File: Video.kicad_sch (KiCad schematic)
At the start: 53 parts, among them Q10 2N3904, Q6 2N3904, Q7 2N3904, Q8 2N3904, Q9 2N3904, U13 74HCT14D, U15 74HC86, U40 GST_SHIFTER, U41 74LS257, U42 GST_MCU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

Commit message: motherboard: Added more footprints for parts and refined the serial comms section further
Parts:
- U41: footprint (none) -> Package_SO:TSSOP-16_4.4x5mm_P0.65mm; MFR (none) -> Nexperia; MPN (none) -> 74HC257PW,118; OC_FARNELL (none) -> 2445284
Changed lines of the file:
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@@
 			)
 		)
-		(property "Footprint" ""
+		(property "Footprint" "Package_SO:TSSOP-16_4.4x5mm_P0.65mm"
 			(at 355.6 76.2 0)
 			(effects
@@
 			(at 355.6 76.2 0)
 			(effects
+				(font
+					(size 1.27 1.27)
+				)
+				(hide yes)
+			)
+		)
+		(property "MFR" "Nexperia"
+			(at 355.6 76.2 0)
+			(effects
+				(font
+					(size 1.27 1.27)
+				)
+				(hide yes)
+			)
+		)
+		(property "MPN" "74HC257PW,118"
+			(at 355.6 76.2 0)
+			(effects
+				(font
+					(size 1.27 1.27)
+				)
+				(hide yes)
+			)
+		)
+		(property "OC_FARNELL" "2445284"
+			(at 355.6 76.2 0)
+			(effects

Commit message: motherboard: Sorted out all the 1N914's having found a suitable part
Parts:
- D8, D9: footprint (none) -> Diode_SMD:D_SOD-323F; MFR (none) -> Onsemi; MPN (none) -> 1N914BWS; OC_FARNELL (none) -> 2453274
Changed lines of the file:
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@@
 			)
 		)
-		(property "Footprint" ""
+		(property "Footprint" "Diode_SMD:D_SOD-323F"
 			(at 238.76 227.33 90)
 			(effects
@@
 			)
 		)
-		(property "Datasheet" "~"
+		(property "Datasheet" "https://www.onsemi.com/download/data-sheet/pdf/1n4148ws-d.pdf"
 			(at 238.76 227.33 90)
 			(effects
@@
 			)
 		)
-		(property "MFR" ""
+		(property "MFR" "Onsemi"
 			(at 238.76 227.33 0)
 			(effects
@@
 			)
 		)
-		(property "MPN" ""
+		(property "MPN" "1N914BWS"
 			(at 238.76 227.33 0)
 			(effects
@@
 			)
 		)
-		(property "OC_FARNELL" ""
+		(property "OC_FARNELL" "2453274"
 			(at 238.76 227.33 0)
 			(effects
@@
 			)
 		)
-		(property "Footprint" ""
+		(property "Footprint" "Diode_SMD:D_SOD-323F"
 			(at 238.76 220.98 90)
 			(effects
@@
 			)
 		)
-		(property "Datasheet" "~"
+		(property "Datasheet" "https://www.onsemi.com/download/data-sheet/pdf/1n4148ws-d.pdf"
 			(at 238.76 220.98 90)
 			(effects
@@
 			)
 		)
-		(property "MFR" ""
+		(property "MFR" "Onsemi"
 			(at 238.76 220.98 0)
 			(effects
@@
 			)
 		)
-		(property "MPN" ""
+		(property "MPN" "1N914BWS"
 			(at 238.76 220.98 0)
 			(effects
@@
 			)
 		)
-		(property "OC_FARNELL" ""
+		(property "OC_FARNELL" "2453274"
 			(at 238.76 220.98 0)
 			(effects

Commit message: motherboard: Sorted out the connectors for the joystick ports and video port
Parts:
- added C126, C127, C128, C129, C130: 100n, rhais_rcl:C0603, symbol Device:C_Small
- added J14: Video, Connector_Dsub:DSUB-15-HD_Socket_Horizontal_P2.29x2.54mm_EdgePinOffset8.35mm_Housed_MountingHolesOffset10.89mm, symbol Connector:DE15_Socket_HighDensity
- added R126, R127: 33R, rhais_rcl:R0603, symbol Device:R_Small
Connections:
- net +5V: now also C126.1, C127.1, C128.1, C129.1, C130.1
- net GND: now also C126.2, C127.2, C128.2, C129.2, C130.2, J14.10, J14.5, J14.6, J14.7, J14.8
- net HSYNC: now also R126.2
- net ~{VSYNC}: now also R127.2
- net R: now reaches R121.2
- net R: now also J14.1
- net B: now reaches R123.2
- net B: now also J14.3
- net G: now reaches R122.2
- net G: now also J14.2
- new net: J14.13, R126.1
- new net: J14.14, R127.1
- no-connect marks 21 -> 27

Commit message: motherboard: Routed in the sound DMA output and microwire control from SHIFTER
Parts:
- removed unit 2 of U13
- added unit 1 of U13
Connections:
- net Sound.D7: now also U13.2
- net at U40.21 (SD7): now also U13.1
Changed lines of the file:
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@@
-	)
-	(symbol
-		(lib_id "74xx:74LS04")
-		(at 243.84 198.12 0)
-		(unit 2)
-		(exclude_from_sim no)
-		(in_bom yes)
-		(on_board yes)
-		(dnp no)
-		(property "Reference" "U13"
-			(at 242.824 198.12 0)
-			(effects
-				(font
-					(size 1.27 1.27)
-				)
-			)
-		)
-		(property "Value" "74HCT14D"
-			(at 246.38 201.93 0)
-			(effects
-				(font
-					(size 1.27 1.27)
-				)
-			)
-		)
-		(property "Footprint" "rhais_package-smd:SO-14_3.9x8.65mm_P1.27mm"
-			(at 243.84 198.12 0)
-			(effects
-				(font
-					(size 1.27 1.27)
-				)
-				(hide yes)
-			)
-		)
-		(property "Datasheet" "https://assets.nexperia.com/documents/data-sheet/74HC_HCT14.pdf"
-			(at 243.84 198.12 0)
-			(effects
-				(font
-					(size 1.27 1.27)
-				)
-				(hide yes)
-			)
-		)
-		(property "Description" "Hex Inverter"
-			(at 243.84 198.12 0)
-			(effects
-				(font
-					(size 1.27 1.27)
-				)
-				(hide yes)
-			)
-		)
-		(property "MFR" "Nexperia"
-			(at 243.84 198.12 0)
-			(effects
-				(font
-					(size 1.27 1.27)
-				)
-				(hide yes)
-			)
-		)
-		(property "MPN" "74HCT14D,653"
-			(at 243.84 198.12 0)
-			(effects
-				(font
-					(size 1.27 1.27)
-				)
-				(hide yes)
-			)
-		)
-		(property "OC_FARNELL" "1201304"
-			(at 243.84 198.12 0)
-			(effects
-				(font
-					(size 1.27 1.27)
-				)
-				(hide yes)
-			)
-		)
-		(pin "12"
-		)
-		(pin "10"
-		)
-		(pin "11"
-		)
-		(pin "8"
-		)
-		(pin "7"
-		)
-		(pin "13"
-		)
-		(pin "14"
-		)
-		(pin "4"
-		)
-		(pin "9"
-		)
-		(pin "2"
-		)
-		(pin "6"
-		)
-		(pin "3"
-		)
-		(pin "5"
-		)
-		(pin "1"
-		)
-		(instances
-			(project "dragonSTe"
-				(path "/6cc81c6b-09a2-4492-8ca2-d80a5c796e77/c7206c05-6723-45c2-9080-55867b906515"
-					(reference "U13")
-					(unit 2)
-				)
-			)
-		)
 	)
 	(symbol
@@
 					(unit 1)
 				)
+			)
+		)
+	)
+	(symbol
+		(lib_id "74xx:74LS04")
+		(at 243.84 198.12 0)
+		(unit 1)
+		(exclude_from_sim no)
+		(in_bom yes)
+		(on_board yes)
+		(dnp no)
+		(property "Reference" "U13"
+			(at 242.824 198.12 0)
+			(effects
+				(font
+					(size 1.27 1.27)
+				)
+			)
+		)
+		(property "Value" "74HCT14D"
+			(at 247.65 201.93 0)
+			(effects
+				(font
+					(size 1.27 1.27)
+				)
+			)
+		)
+		(property "Footprint" "rhais_package-smd:SO-14_3.9x8.65mm_P1.27mm"
+			(at 243.84 198.12 0)
+			(effects
+				(font
+					(size 1.27 1.27)
+				)
+				(hide yes)
+			)
+		)
+		(property "Datasheet" "https://assets.nexperia.com/documents/data-sheet/74HC_HCT14.pdf"
+			(at 243.84 198.12 0)
+			(effects
+				(font
+					(size 1.27 1.27)
+				)
+				(hide yes)
+			)
+		)
+		(property "Description" "Hex Inverter"
+			(at 243.84 198.12 0)
+			(effects
+				(font
+					(size 1.27 1.27)
+				)
+				(hide yes)
+			)
+		)
+		(property "MFR" "Nexperia"
+			(at 243.84 198.12 0)
+			(effects
+				(font
+					(size 1.27 1.27)
+				)
+				(hide yes)
+			)
+		)
+		(property "MPN" "74HCT14D,653"
+			(at 243.84 198.12 0)
+			(effects
+				(font
+					(size 1.27 1.27)
+				)
+				(hide yes)
+			)
+		)
+		(property "OC_FARNELL" "1201304"
+			(at 243.84 198.12 0)
+			(effects
+				(font
+					(size 1.27 1.27)
+				)
+				(hide yes)
+			)
+		)
+		(pin "12"
+		)
+		(pin "10"
+		)
+		(pin "11"
+		)
+		(pin "8"
+		)
+		(pin "7"
+		)
+		(pin "13"
+		)
+		(pin "14"
+		)
+		(pin "4"
+		)
+		(pin "9"
+		)
+		(pin "2"
+		)
+		(pin "6"
+		)
+		(pin "3"
+		)
+		(pin "5"
+		)
+		(pin "1"
+		)
+		(instances
+			(project "dragonSTe"
+				(path "/6cc81c6b-09a2-4492-8ca2-d80a5c796e77/c7206c05-6723-45c2-9080-55867b906515"
+					(reference "U13")
+					(unit 1)
+				)

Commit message: motherboard: Cleaned up the clock tree implementation, specifying and fixing down how to do the 32MHz clock source
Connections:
- net MC renamed MCLK
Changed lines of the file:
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@@
 		)
 	)
-	(label "MC"
+	(label "MCLK"
 		(at 195.58 58.42 0)
 		(effects
@@
 		)
 	)
-	(label "MC"
+	(label "MCLK"
 		(at 373.38 60.96 180)
 		(effects

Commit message: motherboard: Plumbed in MCLK to the mux and SHIFTER
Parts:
- added C132: 100n, rhais_rcl:C0603, symbol Device:C_Small
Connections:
- net +5V: now also C132.1
- net GND: now also C132.2
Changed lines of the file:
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@@
 	(wire
 		(pts
+			(xy 393.7 78.74) (xy 393.7 81.28)
+		)
+		(stroke
+			(width 0)
+			(type default)
+		)
+	)
+	(wire
+		(pts
 			(xy 104.14 177.8) (xy 109.22 177.8)
 		)
@@
 	(wire
 		(pts
+			(xy 393.7 71.12) (xy 393.7 73.66)
+		)
+		(stroke
+			(width 0)
+			(type default)
+		)
+	)
+	(wire
+		(pts
 			(xy 363.22 170.18) (xy 365.76 170.18)
 		)
@@
 	)
 	(symbol
+		(lib_id "power:+5V")
+		(at 393.7 71.12 0)
+		(unit 1)
+		(exclude_from_sim no)
+		(in_bom yes)
+		(on_board yes)
+		(dnp no)
+		(property "Reference" "#PWR0312"
+			(at 393.7 74.93 0)
+			(effects
+				(font
+					(size 1.27 1.27)
+				)
+				(hide yes)
+			)
+		)
+		(property "Value" "+5V"
+			(at 393.7 67.564 0)
+			(effects
+				(font
+					(size 1.27 1.27)
+				)
+			)
+		)
+		(property "Footprint" ""
+			(at 393.7 71.12 0)
+			(effects
+				(font
+					(size 1.27 1.27)
+				)
+				(hide yes)
+			)
+		)
+		(property "Datasheet" ""
+			(at 393.7 71.12 0)
+			(effects
+				(font
+					(size 1.27 1.27)
+				)
+				(hide yes)
+			)
+		)
+		(property "Description" "Power symbol creates a global label with name \"+5V\""
+			(at 393.7 71.12 0)
+			(effects
+				(font
+					(size 1.27 1.27)
+				)
+				(hide yes)
+			)
+		)
+		(pin "1"
+		)
+		(instances
+			(project "dragonSTe"
+				(path "/6cc81c6b-09a2-4492-8ca2-d80a5c796e77/c7206c05-6723-45c2-9080-55867b906515"
+					(reference "#PWR0312")
+					(unit 1)
+				)
+			)
+		)
+	)
+	(symbol
 		(lib_id "Device:C_Small")
 		(at 121.92 50.8 0)
@@
 	)
 	(symbol
+		(lib_id "power:GND")
+		(at 393.7 81.28 0)
+		(unit 1)
+		(exclude_from_sim no)
+		(in_bom yes)
+		(on_board yes)
+		(dnp no)
+		(property "Reference" "#PWR0313"
+			(at 393.7 87.63 0)
+			(effects
+				(font
+					(size 1.27 1.27)
+				)
+				(hide yes)
+			)
+		)
+		(property "Value" "GND"
+			(at 393.7 85.09 0)
+			(effects
+				(font
+					(size 1.27 1.27)
+				)
+			)
+		)
+		(property "Footprint" ""
+			(at 393.7 81.28 0)
+			(effects
+				(font
+					(size 1.27 1.27)
+				)
+				(hide yes)
+			)
+		)
+		(property "Datasheet" ""
+			(at 393.7 81.28 0)
+			(effects
+				(font
+					(size 1.27 1.27)
+				)
+				(hide yes)
+			)
+		)
+		(property "Description" "Power symbol creates a global label with name \"GND\" , ground"
+			(at 393.7 81.28 0)
+			(effects
+				(font
+					(size 1.27 1.27)
+				)
+				(hide yes)
+			)
+		)
+		(pin "1"
+		)
+		(instances
+			(project "dragonSTe"
+				(path "/6cc81c6b-09a2-4492-8ca2-d80a5c796e77/c7206c05-6723-45c2-9080-55867b906515"
+					(reference "#PWR0313")
+					(unit 1)
+				)
+			)
+		)
+	)
+	(symbol
 		(lib_id "Device:R_Small")
 		(at 236.22 63.5 270)
@@
 					(unit 1)
 				)
+			)
+		)
+	)
+	(symbol
+		(lib_id "Device:C_Small")
+		(at 393.7 76.2 0)
+		(unit 1)
+		(exclude_from_sim no)
+		(in_bom yes)
+		(on_board yes)
+		(dnp no)
+		(property "Reference" "C132"
+			(at 393.446 75.438 90)
+			(effects
+				(font
+					(size 1.27 1.27)
+				)
+				(justify left bottom)
+			)
+		)
+		(property "Value" "100n"
+			(at 393.446 76.708 90)
+			(effects
+				(font
+					(size 1.27 1.27)
+				)
+				(justify right bottom)
+			)
+		)
+		(property "Footprint" "rhais_rcl:C0603"
+			(at 393.7 76.2 0)
+			(effects
+				(font
+					(size 1.27 1.27)
+				)
+				(hide yes)
+			)
+		)
+		(property "Datasheet" "~"
+			(at 393.7 76.2 0)
+			(effects
+				(font
+					(size 1.27 1.27)
+				)
+				(hide yes)
+			)
+		)
+		(property "Description" "Unpolarized capacitor, small symbol"
+			(at 393.7 76.2 0)
+			(effects
+				(font
+					(size 1.27 1.27)
+				)
+				(hide yes)
+			)
+		)
+		(property "MFR" ""
+			(at 393.7 76.2 0)
+			(effects
+				(font
+					(size 1.27 1.27)
+				)
+				(hide yes)
+			)
+		)
+		(property "MPN" ""
+			(at 393.7 76.2 0)
+			(effects
+				(font
+					(size 1.27 1.27)
+				)
+				(hide yes)
+			)
+		)
+		(property "OC_FARNELL" ""
+			(at 393.7 76.2 0)
+			(effects
+				(font
+					(size 1.27 1.27)
+				)
+				(hide yes)
+			)
+		)
+		(pin "1"
+		)
+		(pin "2"
+		)
+		(instances
+			(project "dragonSTe"
+				(path "/6cc81c6b-09a2-4492-8ca2-d80a5c796e77/c7206c05-6723-45c2-9080-55867b906515"
+					(reference "C132")
+					(unit 1)
+				)

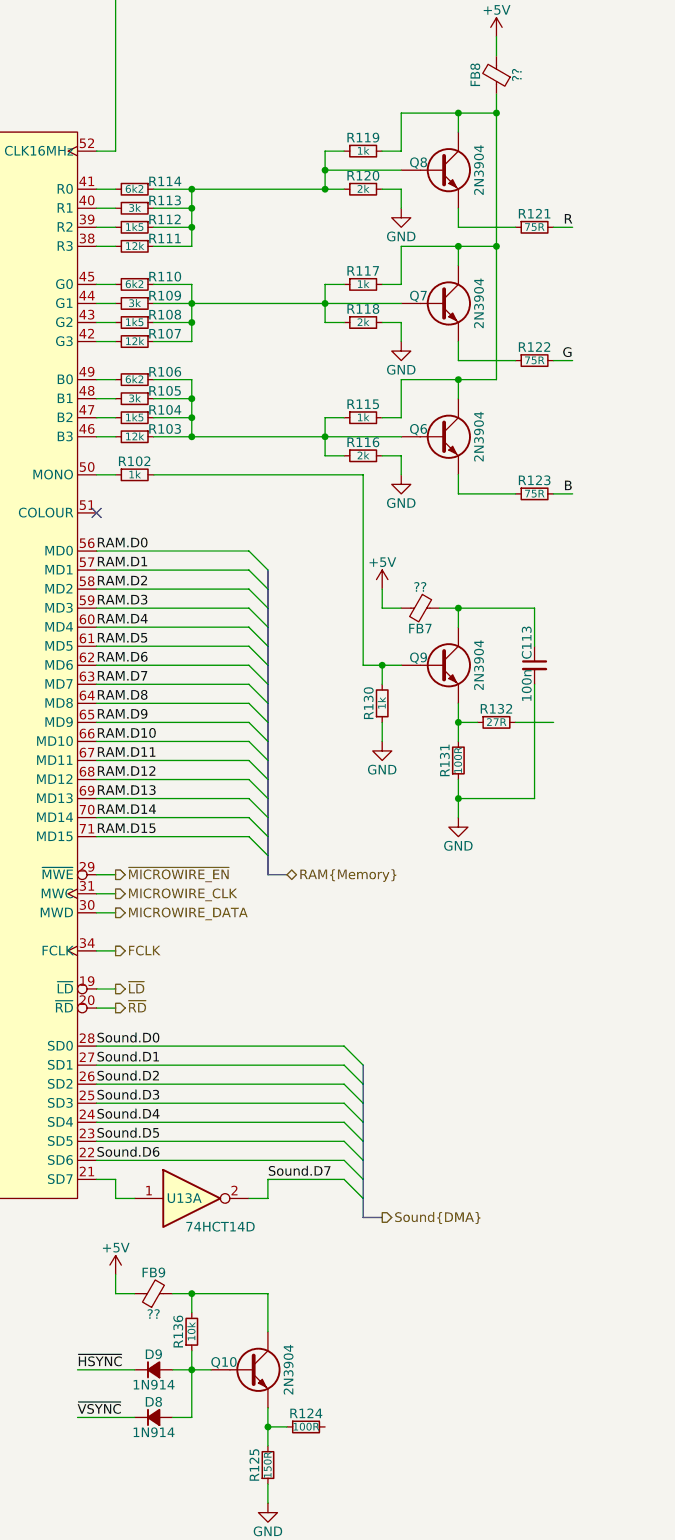
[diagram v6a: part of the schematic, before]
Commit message: motherboard: Routed the video output from SHIFTER
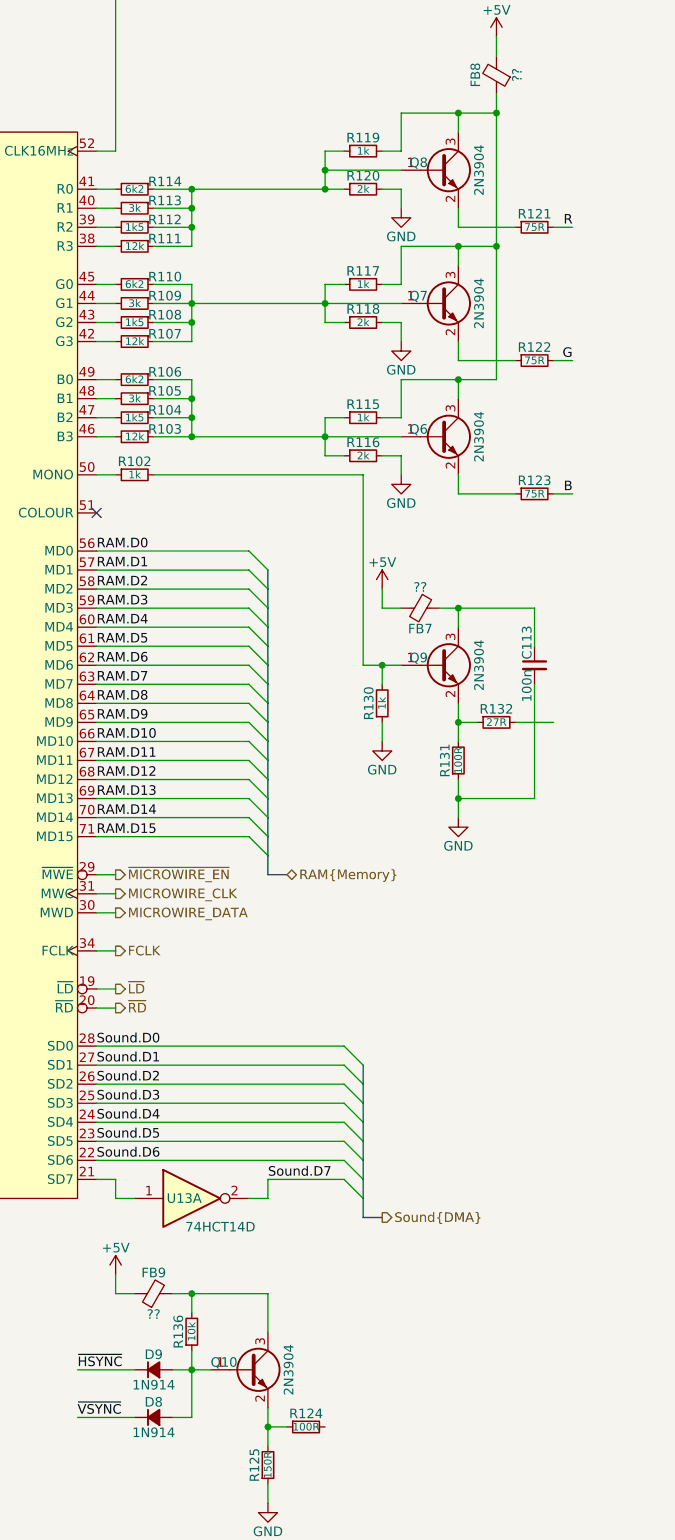
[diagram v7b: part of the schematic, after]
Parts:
- J14: footprint Connector_Dsub:DSUB-15-HD_Socket_Horizontal_P2.29x2.54mm_EdgePinOffset8.35mm_Housed_MountingHolesOffset10.89mm -> rhais_connector-dsub:DSUB-15-HD_Socket_Horizontal_P2.29x2.54mm_EdgePinOffset8.35mm_Housed_MountingHolesOffset10.89mm
- Q10, Q6, Q7, Q8, Q9: symbol Device:Q_NPN -> dragonmux:Q_NPN_BEC; MFR (none) -> Nexperia; MPN (none) -> MMBT3904,215; OC_FARNELL (none) -> 1757935
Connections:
- net at R103.1, R104.1, R105.1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: now also Q6.1 (B); no longer Q6.B
- net at R102.2, R130.2: now also Q9.1 (B); no longer Q9.B
- net at R131.2, R132.1: now also Q9.2 (E); no longer Q9.E
- net at R111.1, R112.1, R113.1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: now also Q8.1 (B); no longer Q8.B
- net at FB8.1, R115.2, R117.2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: now also Q6.3 (C), Q7.3 (C), Q8.3 (C); no longer Q6.C, Q7.C, Q8.C
- net at R121.1: now also Q8.2 (E); no longer Q8.E
- net at R107.1, R108.1, R109.1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: now also Q7.1 (B); no longer Q7.B
- net at R124.1, R125.2: now also Q10.2 (E); no longer Q10.E
- net at D8.2 (A), D9.2 (A), R136.1: now also Q10.1 (B); no longer Q10.B
- net at FB9.2, R136.2: now also Q10.3 (C); no longer Q10.C
- net at R122.1: now also Q7.2 (E); no longer Q7.E
- net at R123.1: now also Q6.2 (E); no longer Q6.E
- net at C113.1, FB7.1: now also Q9.3 (C); no longer Q9.C
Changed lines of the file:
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@@
 	)
 	(symbol
-		(lib_id "Device:Q_NPN")
+		(lib_id "dragonmux:Q_NPN_BEC")
 		(at 276.86 60.96 0)
 		(unit 1)
@@
 			)
 		)
-		(property "Datasheet" "~"
+		(property "Datasheet" "https://assets.nexperia.com/documents/data-sheet/MMBT3904.pdf"
 			(at 276.86 60.96 0)
 			(effects
@@
 			)
 		)
-		(property "MFR" ""
+		(property "MFR" "Nexperia"
 			(at 276.86 60.96 0)
 			(effects
@@
 			)
 		)
-		(property "MPN" ""
+		(property "MPN" "MMBT3904,215"
 			(at 276.86 60.96 0)
 			(effects
@@
 			)
 		)
-		(property "OC_FARNELL" ""
+		(property "OC_FARNELL" "1757935"
 			(at 276.86 60.96 0)
 			(effects
@@
 			)
 		)
-		(pin "B"
+		(pin "1"
 		)
-		(pin "C"
+		(pin "3"
 		)
-		(pin "E"
+		(pin "2"
 		)
 		(instances
@@
 	)
 	(symbol
-		(lib_id "Device:Q_NPN")
+		(lib_id "dragonmux:Q_NPN_BEC")
 		(at 251.46 220.98 0)
 		(unit 1)
@@
 			)
 		)
-		(property "Datasheet" "~"
+		(property "Datasheet" "https://assets.nexperia.com/documents/data-sheet/MMBT3904.pdf"
 			(at 251.46 220.98 0)
 			(effects
@@
 			)
 		)
-		(property "MFR" ""
+		(property "MFR" "Nexperia"
 			(at 251.46 220.98 0)
 			(effects
@@
 			)
 		)
-		(property "MPN" ""
+		(property "MPN" "MMBT3904,215"
 			(at 251.46 220.98 0)
 			(effects
@@
 			)
 		)
-		(property "OC_FARNELL" ""
+		(property "OC_FARNELL" "1757935"
 			(at 251.46 220.98 0)
 			(effects
@@
 			)
 		)
-		(pin "B"
+		(pin "1"
 		)
-		(pin "C"
+		(pin "2"
 		)
-		(pin "E"
+		(pin "3"
 		)
 		(instances
@@
 	)
 	(symbol
-		(lib_id "Device:Q_NPN")
+		(lib_id "dragonmux:Q_NPN_BEC")
 		(at 276.86 78.74 0)
 		(unit 1)
@@
 			)
 		)
-		(property "Datasheet" "~"
+		(property "Datasheet" "https://assets.nexperia.com/documents/data-sheet/MMBT3904.pdf"
 			(at 276.86 78.74 0)
 			(effects
@@
 			)
 		)
-		(property "MFR" ""
+		(property "MFR" "Nexperia"
 			(at 276.86 78.74 0)
 			(effects
@@
 			)
 		)
-		(property "MPN" ""
+		(property "MPN" "MMBT3904,215"
 			(at 276.86 78.74 0)
 			(effects
@@
 			)
 		)
-		(property "OC_FARNELL" ""
+		(property "OC_FARNELL" "1757935"
 			(at 276.86 78.74 0)
 			(effects
@@
 			)
 		)
-		(pin "B"
+		(pin "1"
 		)
-		(pin "C"
+		(pin "3"
 		)
-		(pin "E"
+		(pin "2"
 		)
 		(instances
@@
 	)
 	(symbol
-		(lib_id "Device:Q_NPN")
+		(lib_id "dragonmux:Q_NPN_BEC")
 		(at 276.86 127 0)
 		(unit 1)
@@
 			)
 		)
-		(property "Datasheet" "~"
+		(property "Datasheet" "https://assets.nexperia.com/documents/data-sheet/MMBT3904.pdf"
 			(at 276.86 127 0)
 			(effects
@@
 			)
 		)
-		(property "MFR" ""
+		(property "MFR" "Nexperia"
 			(at 276.86 127 0)
 			(effects
@@
 			)
 		)
-		(property "MPN" ""
+		(property "MPN" "MMBT3904,215"
 			(at 276.86 127 0)
 			(effects
@@
 			)
 		)
-		(property "OC_FARNELL" ""
+		(property "OC_FARNELL" "1757935"
 			(at 276.86 127 0)
 			(effects
@@
 			)
 		)
-		(pin "B"
+		(pin "3"
 		)
-		(pin "C"
+		(pin "2"
 		)
-		(pin "E"
+		(pin "1"
 		)
 		(instances
@@
 			)
 		)
-		(property "Footprint" "Connector_Dsub:DSUB-15-HD_Socket_Horizontal_P2.29x2.54mm_EdgePinOffset8.35mm_Housed_MountingHolesOffset10.89mm"
+		(property "Footprint" "rhais_connector-dsub:DSUB-15-HD_Socket_Horizontal_P2.29x2.54mm_EdgePinOffset8.35mm_Housed_MountingHolesOffset10.89mm"
 			(at 331.47 154.94 0)
 			(effects
@@
 	)
 	(symbol
-		(lib_id "Device:Q_NPN")
+		(lib_id "dragonmux:Q_NPN_BEC")
 		(at 276.86 96.52 0)
 		(unit 1)
@@
 			)
 		)
-		(property "Datasheet" "~"
+		(property "Datasheet" "https://assets.nexperia.com/documents/data-sheet/MMBT3904.pdf"
 			(at 276.86 96.52 0)
 			(effects
@@
 			)
 		)
-		(property "MFR" ""
+		(property "MFR" "Nexperia"
 			(at 276.86 96.52 0)
 			(effects
@@
 			)
 		)
-		(property "MPN" ""
+		(property "MPN" "MMBT3904,215"
 			(at 276.86 96.52 0)
 			(effects
@@
 			)
 		)
-		(property "OC_FARNELL" ""
+		(property "OC_FARNELL" "1757935"
 			(at 276.86 96.52 0)
 			(effects
@@
 			)
 		)
-		(pin "B"
+		(pin "2"
 		)
-		(pin "C"
+		(pin "1"
 		)
-		(pin "E"
+		(pin "3"
 		)
 		(instances

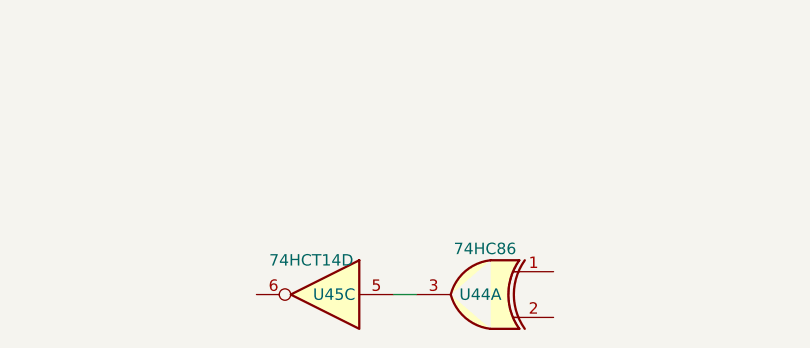
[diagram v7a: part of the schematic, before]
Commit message: motherboard: Routed in the last of the HDD control buffers, and begun routing in BLiTTER
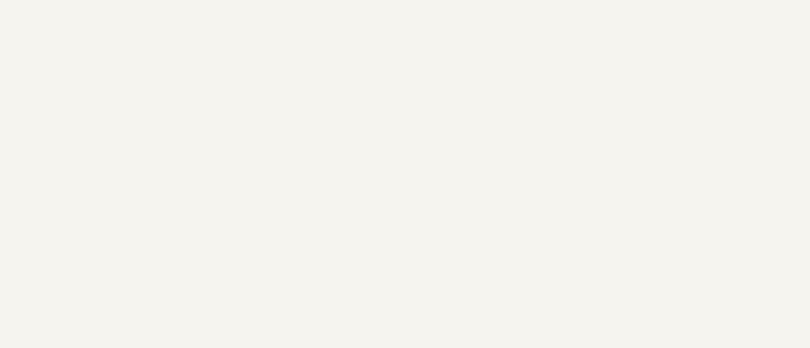
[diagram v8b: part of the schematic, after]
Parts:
- removed U44: 74HC86, rhais_package-smd:SO-14_3.9x8.65mm_P1.27mm, symbol 74xx:74LS86
- removed U45: 74HCT14D, rhais_package-smd:SO-14_3.9x8.65mm_P1.27mm, symbol 74xx:74LS04
